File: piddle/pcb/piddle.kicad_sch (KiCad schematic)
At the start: 48 parts, among them J1 Conn_01x03_Socket, J10 Conn_01x03_Socket, J11 Conn_01x02_Socket, J12 Conn_01x02_Socket, J13 Conn_01x02_Pin, J2 Conn_01x03_Socket, J3 Conn_01x03_Socket, J4 Conn_01x03_Socket, J5 Conn_01x03_Socket, J6 Conn_01x03_Socket, J7 Conn_01x03_Socket, J8 Conn_01x03_Socket, J9 Conn_01x03_Socket, U1 ESP32-DevKitC, U2 INMP441

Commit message: Start 15 pin
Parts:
- removed C1: 0.1uF, Capacitor_THT:C_Disc_D10.0mm_W2.5mm_P5.00mm, symbol Device:C
- removed D10, D14, D16, D18, D2, D20, D4, D6, D8: 1N4148, Diode_THT:D_DO-35_SOD27_P10.16mm_Horizontal, symbol Diode:1N4148
- added D10, D2, D4, D6, D8: WS2812B, LED_SMD:LED_WS2812B_PLCC4_5.0x5.0mm_P3.2mm, symbol LED:WS2812B
- added J14, J15, J16, J17, J18: Conn_01x03_Socket, Connector_PinHeader_2.54mm:PinHeader_1x03_P2.54mm_Vertical, symbol Connector:Conn_01x03_Socket
- added R13, R14, R15: 400, Resistor_THT:R_Axial_DIN0207_L6.3mm_D2.5mm_P10.16mm_Horizontal, symbol Device:R
- R11, R12: value 10000 -> 400
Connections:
- net +5V: no longer R11.1
- net GND: now also D10.3 (VSS), D2.3 (VSS), D4.3 (VSS), D6.3 (VSS), D8.3 (VSS), J14.1 (Pin_1), J15.1 (Pin_1), J16.1 (Pin_1), J17.1 (Pin_1), J18.1 (Pin_1); no longer R12.2
- net GPIO12: now also R2.1; no longer R4.1
- net GPIO13: now also R1.1; no longer R5.1
- net GPIO14: now also R3.1
- net GPIO16: now also R15.2; no longer R7.2
- net GPIO17: now also R14.2; no longer R8.2
- net GPIO18: now also R13.2
- net GPIO19: now also R12.2
- net GPIO21: now also R11.2; no longer R9.2
- net GPIO22: now also R6.2; no longer R10.2
- net GPIO23: now also R7.2
- net GPIO25: now also R10.2; no longer R1.1
- net GPIO26: now also R5.1; no longer R2.1
- net GPIO27: now also R4.1; no longer R3.1
- net GPIO32: now also R8.2
- net GPIO33: now also R9.2
- net GPIO4: no longer R6.2
- net 4.3V: now reaches D11.1 (VDD), D12.1 (K)
- net 4.3V: now also D1.1 (VDD), D13.1 (VDD), D15.1 (VDD), D17.1 (VDD), D19.1 (VDD), D3.1 (VDD), D5.1 (VDD), D7.1 (VDD), D9.1 (VDD), D10.1 (VDD), D2.1 (VDD), D4.1 (VDD), D6.1 (VDD), D8.1 (VDD)
- net at J7.2 (Pin_2): now also D13.4 (DIN); no longer D13.2 (DOUT)
- net at R12.1: now also D4.2 (DOUT); no longer R11.2
- net at R7.1: now also D13.2 (DOUT); no longer D13.4 (DIN)
- new net: D10.2 (DOUT), J18.2 (Pin_2)
- new net: D10.4 (DIN), R15.1
- new net: D6.2 (DOUT), J16.2 (Pin_2)
- new net: D8.4 (DIN), R14.1
- new net: D2.2 (DOUT), J14.2 (Pin_2)
- new net: D2.4 (DIN), R11.1
- new net: D8.2 (DOUT), J17.2 (Pin_2)
- new net: D6.4 (DIN), R13.1
- new net: D4.4 (DIN), J15.2 (Pin_2)
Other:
- moved on the sheet: D12

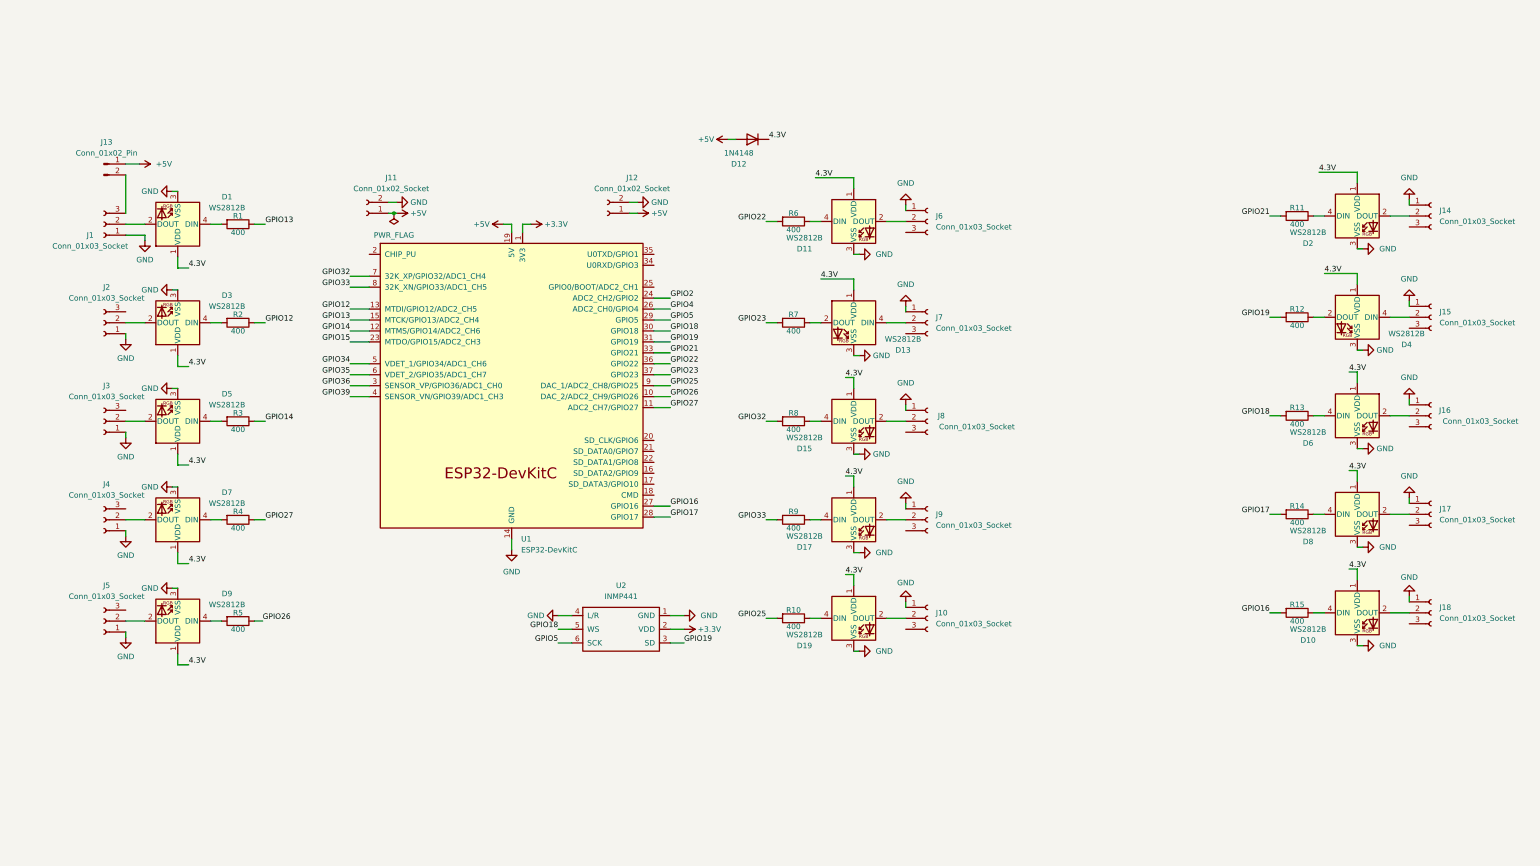
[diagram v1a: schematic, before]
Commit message: Arrange components for 15-strip board
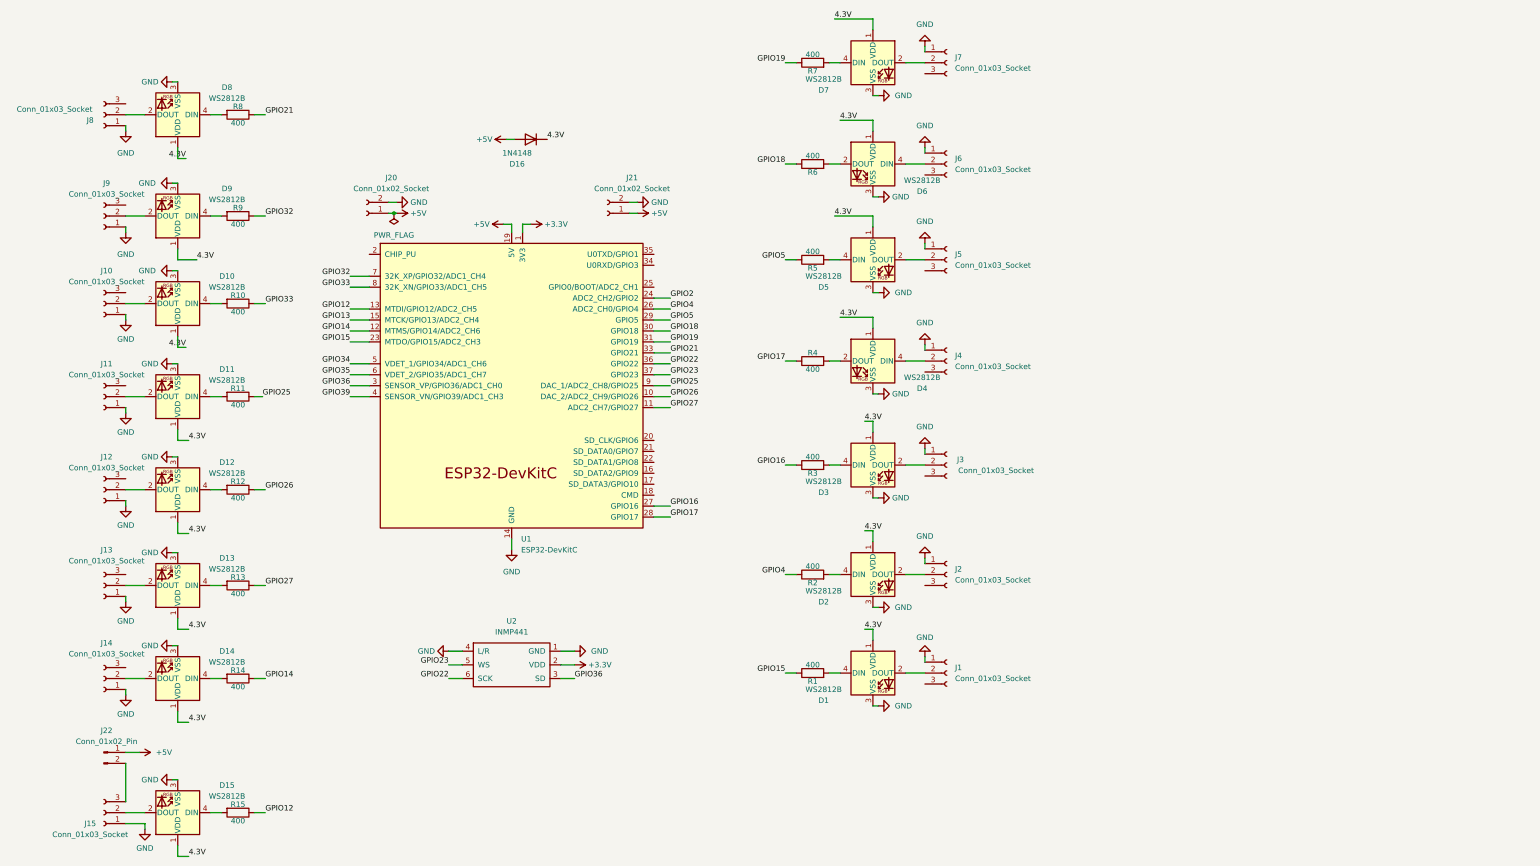
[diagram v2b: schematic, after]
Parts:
- renumbered D10 to D1, D19 to D10, D9 to D11, D7 to D12, D5 to D13, D3 to D14, D1 to D15, D12 to D16, D8 to D2, D6 to D3, D2 to D5, D13 to D6, D11 to D7, D15 to D8, D17 to D9, J18 to J1, J5 to J11, J4 to J12, J3 to J13, J2 to J14, J1 to J15, J17 to J2, J11 to J20, J12 to J21, J13 to J22, J16 to J3, J15 to J4, J14 to J5, J7 to J6, J6 to J7, R15 to R1, R5 to R11, R4 to R12, R3 to R13, R2 to R14, R1 to R15, R14 to R2, R13 to R3, R12 to R4, R11 to R5, R7 to R6, R6 to R7
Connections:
- net GPIO12: now also R15.1; no longer R14.1
- net GPIO13: no longer R15.1
- net GPIO14: now also R14.1; no longer R13.1
- net GPIO15: now also R1.1
- net GPIO16: now also R3.1; no longer R1.2
- net GPIO17: now also R4.1; no longer R2.2
- net GPIO18: now also R6.1; no longer R3.2, U2.5 (WS)
- net GPIO19: now also R7.1; no longer R4.2, U2.3 (SD)
- net GPIO21: now also R8.1; no longer R5.2
- net GPIO22: now also U2.6 (SCK); no longer R7.2
- net GPIO23: now also U2.5 (WS); no longer R6.2
- net GPIO25: now also R11.1; no longer R10.2
- net GPIO26: now also R12.1; no longer R11.1
- net GPIO27: now also R13.1; no longer R12.1
- net GPIO32: now also R9.1; no longer R8.2
- net GPIO33: now also R10.1; no longer R9.2
- net GPIO36: now also U2.3 (SD)
- net GPIO4: now also R2.1
- net GPIO5: now also R5.1; no longer U2.6 (SCK)
- net at D1.4 (DIN): now also R1.2; no longer R1.1
- net at D2.4 (DIN): now also R2.2; no longer R2.1
- net at D4.2 (DOUT): now also R4.2; no longer R4.1
- net at D10.4 (DIN): now also R10.2; no longer R10.1
- net at D5.4 (DIN): now also R5.2; no longer R5.1
- net at D3.4 (DIN): now also R3.2; no longer R3.1
- net at D7.4 (DIN): now also R7.2; no longer R7.1
- net at D6.2 (DOUT): now also R6.2; no longer R6.1
- net at D9.4 (DIN): now also R9.2; no longer R9.1
- net at D8.4 (DIN): now also R8.2; no longer R8.1
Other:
- moved on the sheet: D1, D10, D11, D12, D13, D14, D15, D16, D2, D3, D4, D5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

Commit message: Add more headers for extra GPIOs, power, remote control
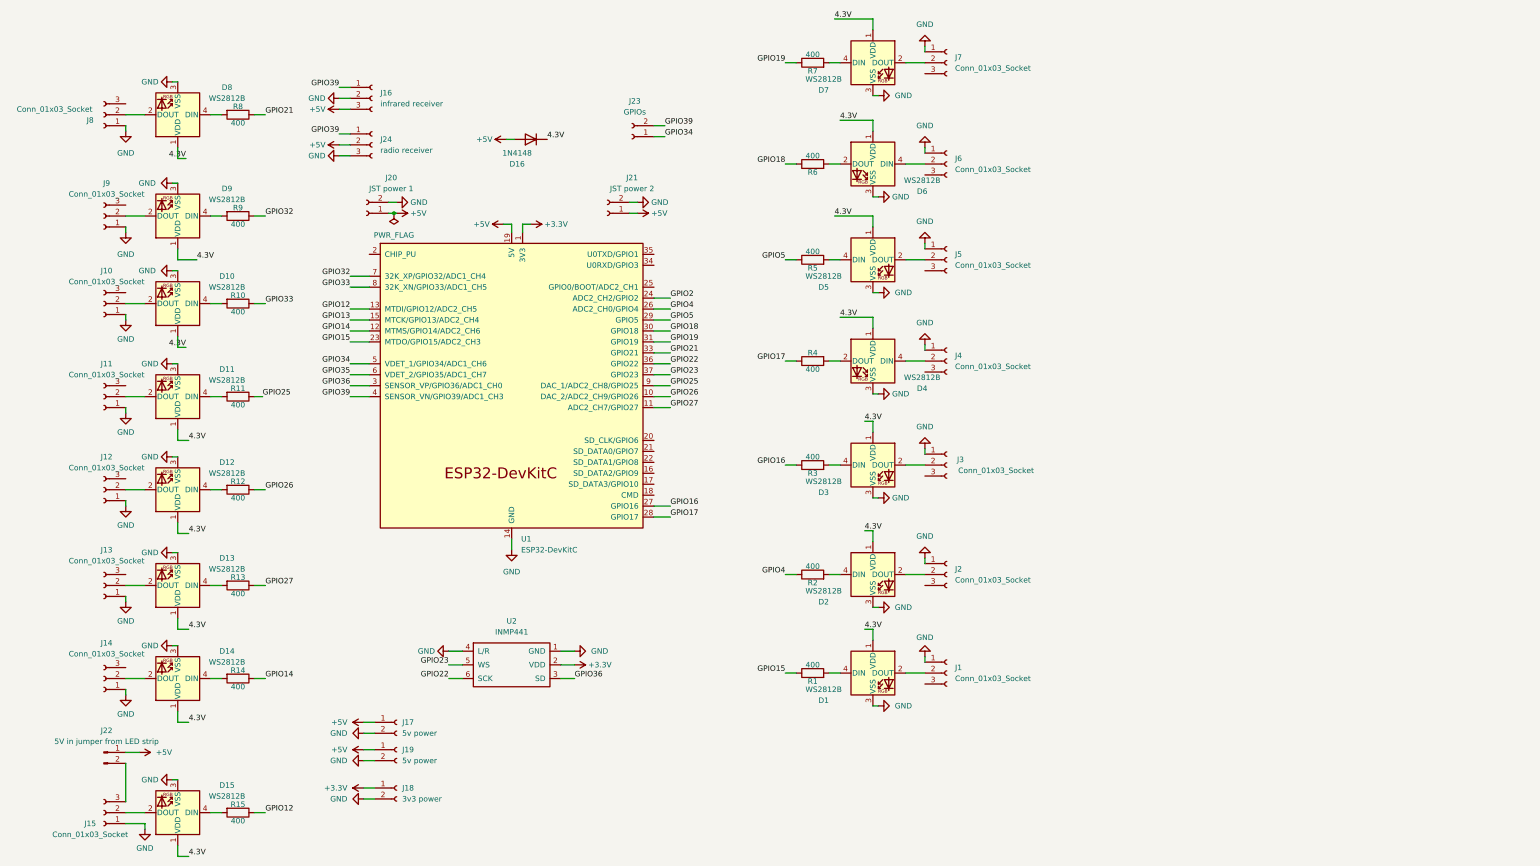
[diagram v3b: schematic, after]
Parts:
- added J16: infrared receiver, Connector_PinHeader_2.54mm:PinHeader_1x03_P2.54mm_Vertical, symbol Connector:Conn_01x03_Socket
- added J17, J19: 5v power, Connector_PinHeader_2.54mm:PinHeader_1x02_P2.54mm_Vertical, symbol Connector:Conn_01x02_Socket
- added J18: 3v3 power, Connector_PinHeader_2.54mm:PinHeader_1x02_P2.54mm_Vertical, symbol Connector:Conn_01x02_Socket
- added J23: GPIOs, Connector_PinHeader_2.54mm:PinHeader_1x02_P2.54mm_Vertical, symbol Connector:Conn_01x02_Socket
- added J24: radio receiver, Connector_PinHeader_2.54mm:PinHeader_1x03_P2.54mm_Vertical, symbol Connector:Conn_01x03_Socket
- J20: value Conn_01x02_Socket -> JST power 1
- J21: value Conn_01x02_Socket -> JST power 2
- J22: value Conn_01x02_Pin -> 5V in jumper from LED strip
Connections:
- net +3.3V: now also J18.1 (Pin_1)
- net +5V: now also J16.3 (Pin_3), J17.1 (Pin_1), J19.1 (Pin_1), J24.2 (Pin_2)
- net GND: now also J16.2 (Pin_2), J17.2 (Pin_2), J18.2 (Pin_2), J19.2 (Pin_2), J24.3 (Pin_3)
- net GPIO34: now also J23.1 (Pin_1)
- net GPIO39: now also J16.1 (Pin_1), J23.2 (Pin_2), J24.1 (Pin_1)

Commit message: Connect all components
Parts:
- added J25: JST power 3, Connector_JST:JST_PH_S2B-PH-K_1x02_P2.00mm_Horizontal, symbol Connector:Conn_01x02_Socket
- J17, J19: value 5v power -> 5v
- J18: value 3v3 power -> 3v3
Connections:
- net +5V: now also J25.1 (Pin_1)
- net GND: now also J25.2 (Pin_2)
- net GPIO34: now also J23.2 (Pin_2); no longer J23.1 (Pin_1)
- net GPIO35: now also J23.1 (Pin_1)
- net GPIO39: no longer J23.2 (Pin_2)
- net at J6.2 (Pin_2): now also D6.2 (DOUT); no longer D6.4 (DIN)
- net at R4.2: now also D4.4 (DIN); no longer D4.2 (DOUT)
- net at R6.2: now also D6.4 (DIN); no longer D6.2 (DOUT)
- net at J4.2 (Pin_2): now also D4.2 (DOUT); no longer D4.4 (DIN)
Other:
- moved on the sheet: D16, J20, J21

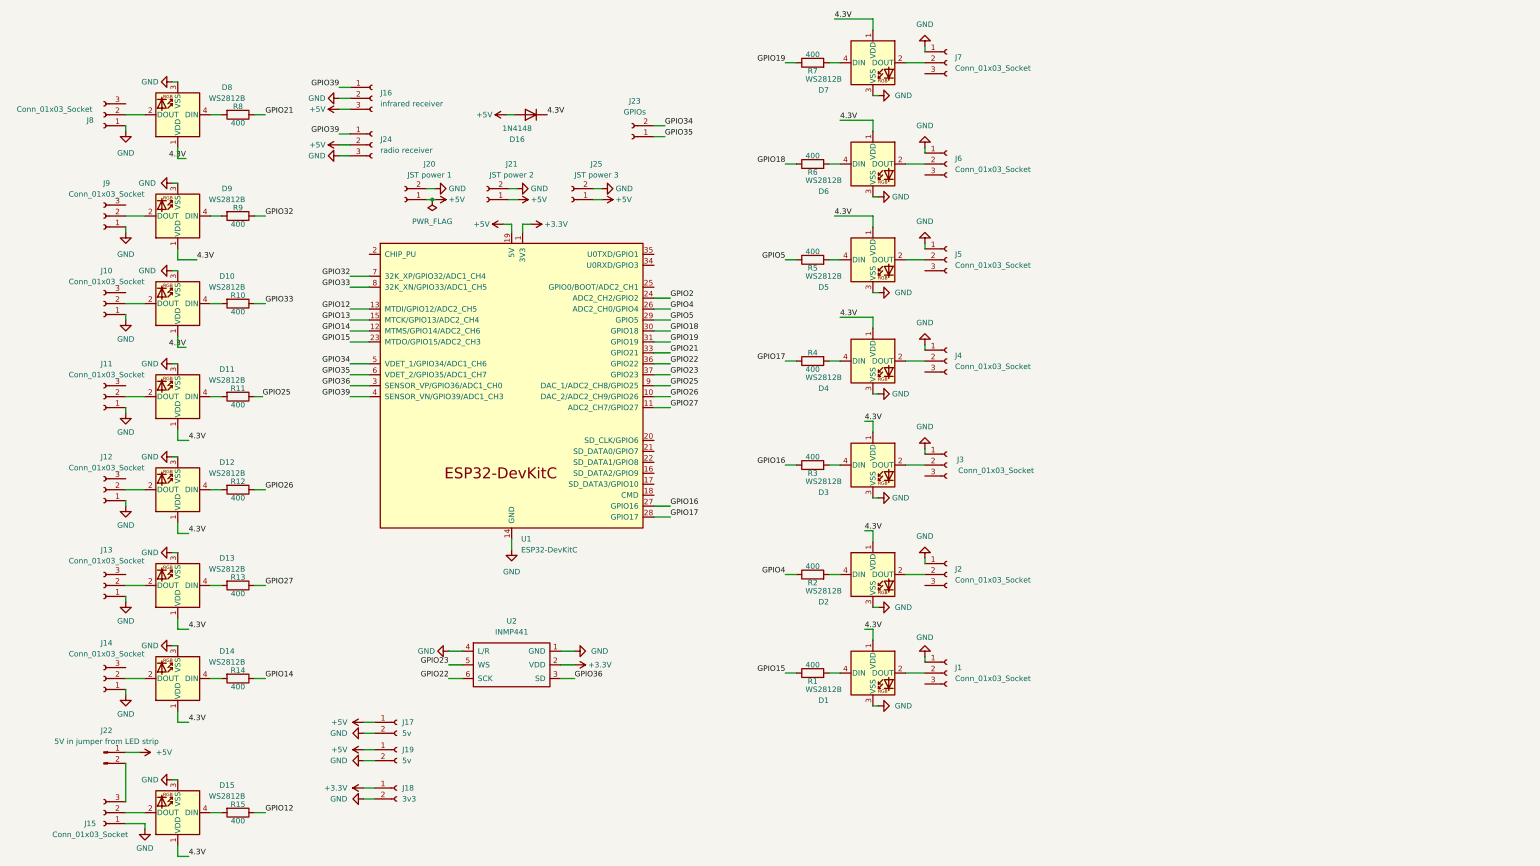
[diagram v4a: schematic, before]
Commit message: Avoid using GPIO 25 and 26 - they're used by DAC (and thus WiFi)
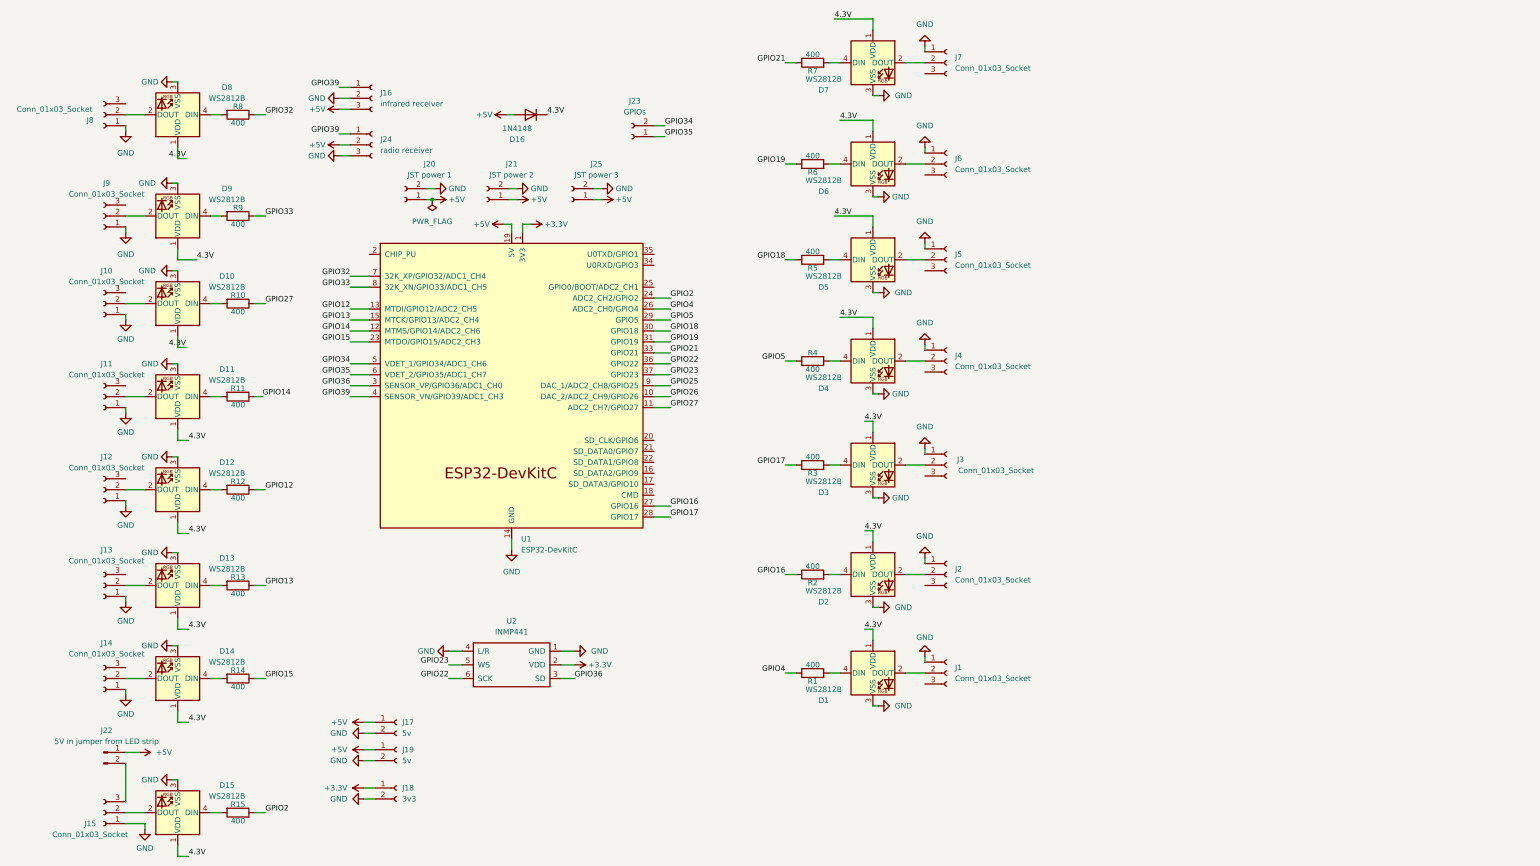
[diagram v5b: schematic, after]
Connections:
- net GPIO12: now also R12.1; no longer R15.1
- net GPIO13: now also R13.1
- net GPIO14: now also R11.1; no longer R14.1
- net GPIO15: now also R14.1; no longer R1.1
- net GPIO16: now also R2.1; no longer R3.1
- net GPIO17: now also R3.1; no longer R4.1
- net GPIO18: now also R5.1; no longer R6.1
- net GPIO19: now also R6.1; no longer R7.1
- net GPIO2: now also R15.1
- net GPIO21: now also R7.1; no longer R8.1
- net GPIO25: no longer R11.1
- net GPIO26: no longer R12.1
- net GPIO27: now also R10.1; no longer R13.1
- net GPIO32: now also R8.1; no longer R9.1
- net GPIO33: now also R9.1; no longer R10.1
- net GPIO4: now also R1.1; no longer R2.1
- net GPIO5: now also R4.1; no longer R5.1
